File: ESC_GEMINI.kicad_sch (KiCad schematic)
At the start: 19 parts, among them P7 Solder Pad, P8 Solder Pad

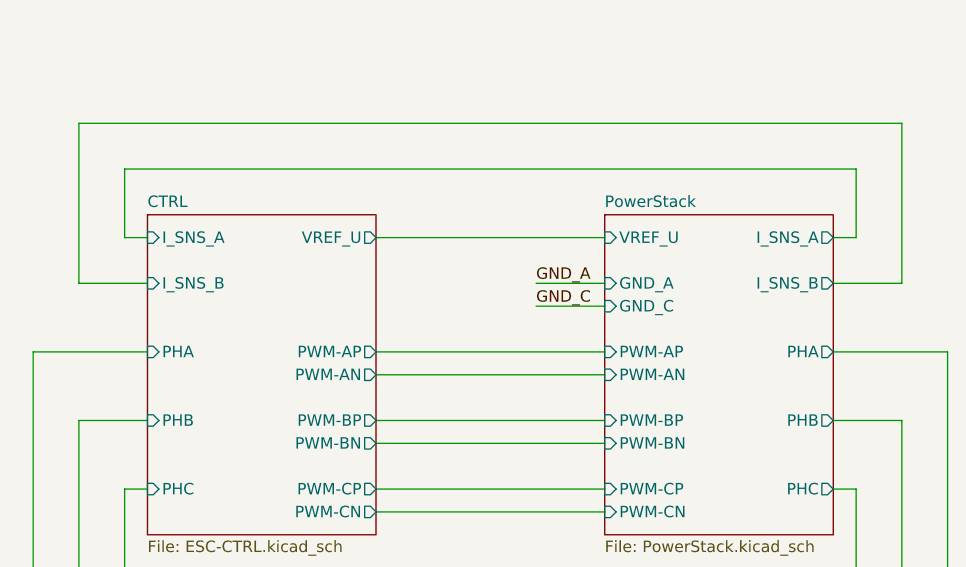
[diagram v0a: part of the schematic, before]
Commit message: Update layout and modified sense amplifier
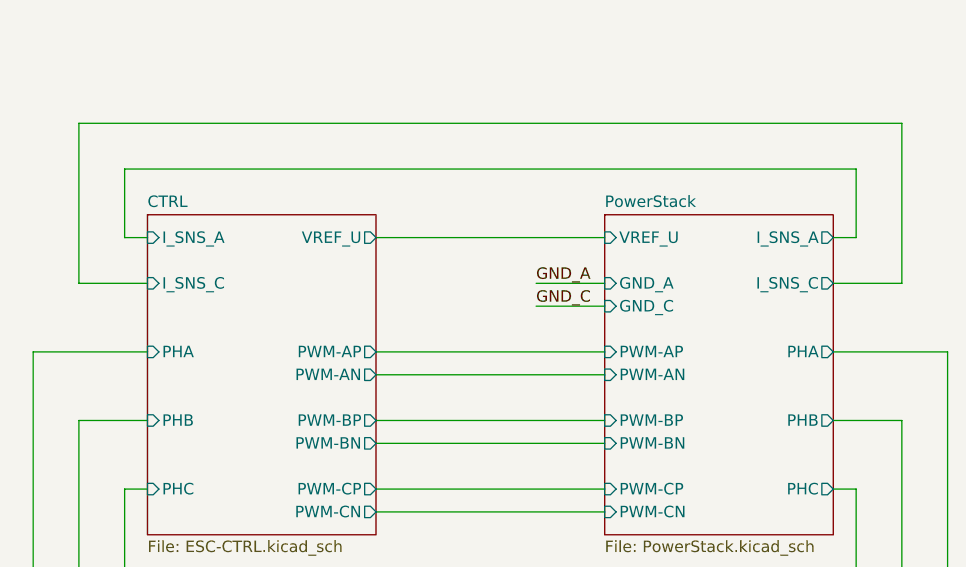
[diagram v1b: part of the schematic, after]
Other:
- sheet CTRL ports: added I_SNS_C; removed I_SNS_B
- sheet PowerStack ports: added I_SNS_C; removed I_SNS_B
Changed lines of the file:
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@@
       (effects (font (size 1.27 1.27)) (justify right))
     )
-    (pin "I_SNS_B" output (at 228.6 99.06 0)
+    (pin "I_SNS_C" output (at 228.6 99.06 0)
       (effects (font (size 1.27 1.27)) (justify right))
     )
@@
       (effects (font (size 1.27 1.27)) (justify left))
     )
-    (pin "I_SNS_B" input (at 152.4 99.06 180)
+    (pin "I_SNS_C" input (at 152.4 99.06 180)
       (effects (font (size 1.27 1.27)) (justify left))
     )

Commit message: Modified the scheme of current sensing
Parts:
- P7, P8: now left out of the parts list
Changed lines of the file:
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@@
   )
   (symbol (lib_id "301_Link_Pad:Pad_Square") (at 121.92 55.88 0) (unit 1)
-    (in_bom yes) (on_board yes) (dnp no) (fields_autoplaced)
+    (in_bom no) (on_board yes) (dnp no) (fields_autoplaced)
     (property "Reference" "P8" (at 124.46 54.61 0)
       (effects (font (size 1.27 1.27)) (justify left))
@@
   )
   (symbol (lib_id "301_Link_Pad:Pad_Square") (at 121.92 45.72 0) (unit 1)
-    (in_bom yes) (on_board yes) (dnp no) (fields_autoplaced)
+    (in_bom no) (on_board yes) (dnp no) (fields_autoplaced)
     (property "Reference" "P7" (at 124.46 44.45 0)
       (effects (font (size 1.27 1.27)) (justify left))
